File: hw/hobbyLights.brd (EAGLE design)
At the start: 50 x 35.1 mm, 57 parts, among them U1 MCP73831-2, U2 POWER, U3 BD48K28G, U4 ATMEGA32U4-AU, U5 TPS61222, Y1 RESONATORSMD

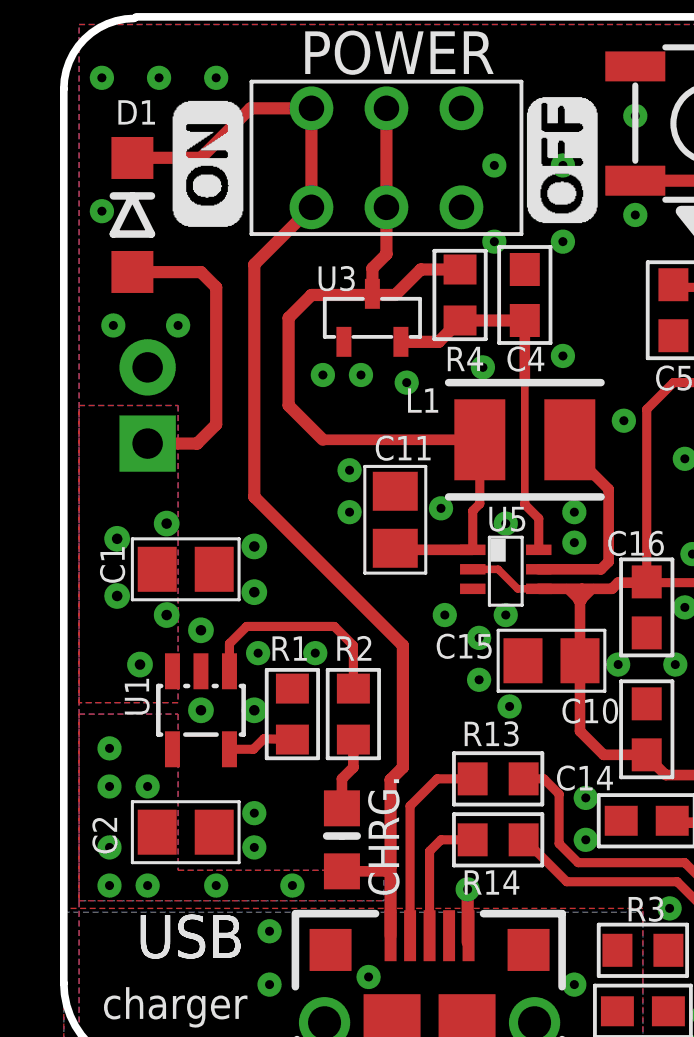
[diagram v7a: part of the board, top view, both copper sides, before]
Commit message: Updated to use JST PH connector. Updates to serigraphy.
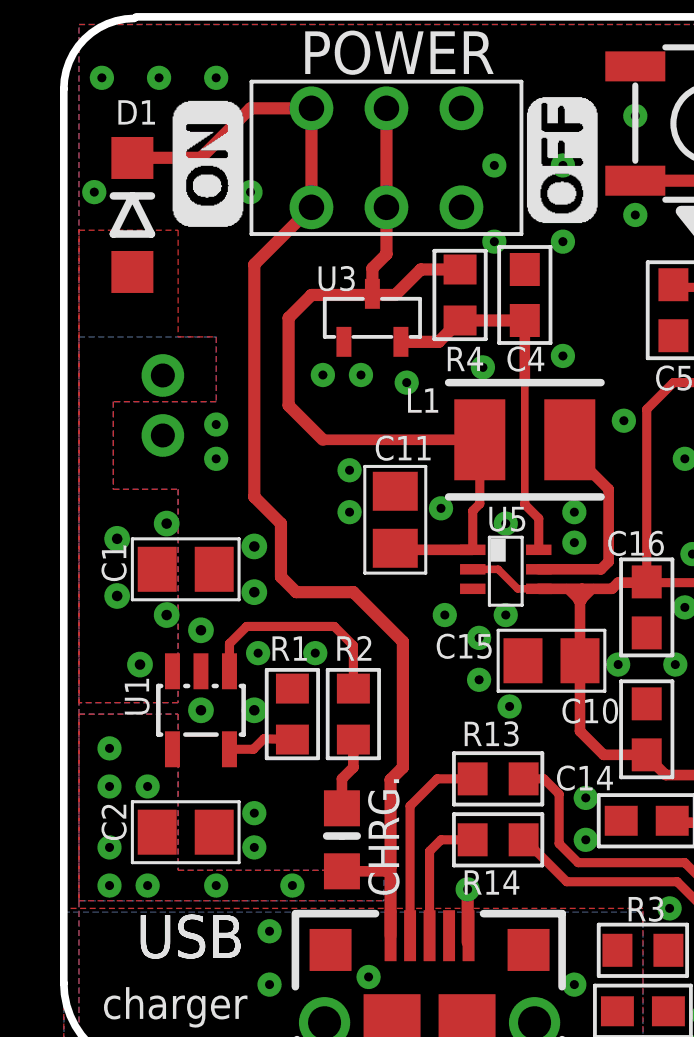
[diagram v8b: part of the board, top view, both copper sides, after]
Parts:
- removed JP1: (no value), SAVLibSAV MK-I:SPARKFUN_MOLEX-1X2
- added CN1: (no value), adafruit:JST-PH-2-THM-RA
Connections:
- net GND: now also CN1.2; no longer JP1.2
- net VCCINT: now also CN1.1; no longer JP1.1
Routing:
- net VCCINT: track 10.1 -> 0.00 mm
- net V_USB: track 38.9 -> 40.0 mm
- net GND: vias 106 -> 107
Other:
- board text added: "B.1"
- board text removed: "B"
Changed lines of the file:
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@@
 <grid distance="0.05" unitdist="inch" unit="mm" style="lines" multiple="1" display="yes" altdistance="5" altunitdist="mil" altunit="mm"/>
 <layers>
-<layer number="1" name="Top" color="4" fill="1" visible="yes" active="yes"/>
+<layer number="1" name="Top" color="4" fill="1" visible="no" active="yes"/>
 <layer number="2" name="Route2" color="1" fill="3" visible="no" active="no"/>
 <layer number="15" name="Route15" color="4" fill="6" visible="no" active="no"/>
-<layer number="16" name="Bottom" color="1" fill="1" visible="no" active="yes"/>
+<layer number="16" name="Bottom" color="1" fill="1" visible="yes" active="yes"/>
 <layer number="17" name="Pads" color="2" fill="1" visible="yes" active="yes"/>
 <layer number="18" name="Vias" color="2" fill="1" visible="yes" active="yes"/>
 <layer number="19" name="Unrouted" color="6" fill="1" visible="yes" active="yes"/>
 <layer number="20" name="Dimension" color="15" fill="1" visible="yes" active="yes"/>
-<layer number="21" name="tPlace" color="7" fill="1" visible="yes" active="yes"/>
-<layer number="22" name="bPlace" color="7" fill="1" visible="no" active="yes"/>
-<layer number="23" name="tOrigins" color="15" fill="1" visible="yes" active="yes"/>
-<layer number="24" name="bOrigins" color="15" fill="1" visible="no" active="yes"/>
-<layer number="25" name="tNames" color="7" fill="1" visible="yes" active="yes"/>
-<layer number="26" name="bNames" color="7" fill="1" visible="no" active="yes"/>
+<layer number="21" name="tPlace" color="7" fill="1" visible="no" active="yes"/>
+<layer number="22" name="bPlace" color="7" fill="1" visible="yes" active="yes"/>
+<layer number="23" name="tOrigins" color="15" fill="1" visible="no" active="yes"/>
+<layer number="24" name="bOrigins" color="15" fill="1" visible="yes" active="yes"/>
+<layer number="25" name="tNames" color="7" fill="1" visible="no" active="yes"/>
+<layer number="26" name="bNames" color="7" fill="1" visible="yes" active="yes"/>
 <layer number="27" name="tValues" color="7" fill="1" visible="no" active="yes"/>
 <layer number="28" name="bValues" color="7" fill="1" visible="no" active="yes"/>
@@
 <wire x1="2.35229375" y1="35" x2="0" y2="32.64770625" width="0.254" layer="20" curve="90"/>
 <wire x1="8.763" y1="7.747" x2="9.779" y2="7.747" width="0.254" layer="21"/>
-<text x="7.747" y="22.606" size="1.778" layer="22" font="vector" ratio="15" rot="MR0">-</text>
-<text x="7.747" y="19.812" size="1.778" layer="22" font="vector" ratio="15" rot="MR0">+</text>
+<text x="6.985" y="18.161" size="2.54" layer="22" font="vector" ratio="15" rot="MR0">-</text>
+<text x="6.985" y="24.13" size="2.54" layer="22" font="vector" ratio="15" rot="MR0">+</text>
 <text x="33.655" y="15.24" size="1.4224" layer="22" font="vector" ratio="12" rot="MR0">hobby lights</text>
-<text x="33.02" y="11.811" size="1.4224" layer="22" font="vector" ratio="12" rot="MR0">B</text>
+<text x="33.02" y="11.811" size="1.4224" layer="22" font="vector" ratio="12" rot="MR0">B.1</text>
 <dimension x1="2.35229375" y1="35" x2="5.08" y2="0" x3="-6.35" y3="17.5" textsize="1.4224" textratio="12" layer="47" dtype="vertical"/>
 <dimension x1="0" y1="32.64770625" x2="50.038" y2="29.21" x3="25.019" y3="39.878" textsize="1.4224" textratio="12" layer="47" dtype="horizontal"/>
@@
 </element>
 <element name="C1" library="rcl" package="C0805" value="4.7uF" x="4.064" y="16.637" smashed="yes">
-<attribute name="NAME" x="2.032" y="16.129" size="0.8128" layer="25" ratio="12" rot="R90"/>
+<attribute name="NAME" x="1.27" y="17.526" size="0.8128" layer="25" ratio="12" rot="R270"/>
 <attribute name="VALUE" x="2.794" y="14.097" size="1.27" layer="27"/>
 </element>
 <element name="C2" library="rcl" package="C0805" value="4.7uF" x="4.064" y="7.874" smashed="yes">
-<attribute name="NAME" x="1.778" y="7.112" size="0.8128" layer="25" ratio="12" rot="R90"/>
+<attribute name="NAME" x="1.27" y="8.89" size="0.8128" layer="25" ratio="12" rot="R270"/>
 <attribute name="VALUE" x="2.794" y="5.334" size="1.27" layer="27"/>
 </element>
@@
 <attribute name="VALUE" x="18.034" y="-0.635" size="1.27" layer="27"/>
 </element>
-<element name="JP1" library="SAVLibSAV MK-I" package="SPARKFUN_MOLEX-1X2" value="" x="2.794" y="20.828" rot="MR90"/>
 <element name="U2" library="fmc" package="SWITCH-JS202011" value="POWER" x="8.255" y="30.353" smashed="yes"/>
 <element name="U$2" library="fmc" package="ON" value="" x="5.969" y="28.067" rot="R90"/>
@@
 <attribute name="NAME" x="31.623" y="1.27" size="0.8128" layer="25" ratio="12"/>
 <attribute name="VALUE" x="27.432" y="-0.254" size="0.8128" layer="27" ratio="12"/>
+</element>
+<element name="CN1" library="adafruit" package="JST-PH-2-THM-RA" value="" x="3.302" y="22.098" smashed="yes" rot="MR90">
+<attribute name="NAME" x="4.097" y="18.425" size="0.8128" layer="26" font="vector" ratio="12" rot="MR0"/>
 </element>
 </elements>
@@
 <via x="13.462" y="5.969" extent="1-16" drill="0.3"/>
 <wire x1="13.462" y1="4.199" x2="13.462" y2="5.969" width="0.4064" layer="1"/>
-<contactref element="JP1" pad="2"/>
 <contactref element="U3" pad="1"/>
 <contactref element="C4" pad="2"/>
@@
 <via x="3.175" y="33.02" extent="1-16" drill="0.3"/>
 <via x="5.08" y="33.02" extent="1-16" drill="0.3"/>
-<via x="1.27" y="28.575" extent="1-16" drill="0.3"/>
-<via x="3.81" y="24.765" extent="1-16" drill="0.3"/>
-<via x="1.651" y="24.765" extent="1-16" drill="0.3"/>
+<via x="1.016" y="29.21" extent="1-16" drill="0.3"/>
 <via x="46.99" y="5.08" extent="1-16" drill="0.3"/>
 <via x="43.18" y="6.35" extent="1-16" drill="0.3"/>
@@
 <via x="39.37" y="22.352" extent="1-16" drill="0.3"/>
 <via x="29.21" y="21.971" extent="1-16" drill="0.3"/>
+<contactref element="CN1" pad="2"/>
+<via x="5.08" y="21.463" extent="1-16" drill="0.3"/>
+<via x="5.08" y="20.32" extent="1-16" drill="0.3"/>
+<via x="6.223" y="29.21" extent="1-16" drill="0.3"/>
 </signal>
 <signal name="N$4">
@@
 <via x="5.08" y="6.096" extent="1-16" drill="0.3"/>
 <via x="7.62" y="6.096" extent="1-16" drill="0.3"/>
-<wire x1="11.303" y1="14.097" x2="11.303" y2="10.033" width="0.4064" layer="1"/>
+<wire x1="11.303" y1="14.224" x2="11.303" y2="10.033" width="0.4064" layer="1"/>
 <contactref element="U2" pad="P4"/>
 <contactref element="U2" pad="P1"/>
 <contactref element="D1" pad="C"/>
-<wire x1="11.303" y1="14.097" x2="6.35" y2="19.05" width="0.4064" layer="1"/>
 <wire x1="8.255" y1="32.003" x2="6.222" y2="32.003" width="0.4064" layer="1"/>
 <wire x1="6.222" y1="32.003" x2="4.572" y2="30.353" width="0.4064" layer="1"/>
@@
 <wire x1="9.271" y1="6.57" x2="10.731" y2="6.57" width="0.3556" layer="1"/>
 <wire x1="10.731" y1="6.57" x2="10.892" y2="6.731" width="0.3556" layer="1"/>
+<wire x1="11.303" y1="14.224" x2="9.652" y2="15.875" width="0.4064" layer="1"/>
+<wire x1="9.652" y1="15.875" x2="7.747" y2="15.875" width="0.4064" layer="1"/>
+<wire x1="7.747" y1="15.875" x2="7.239" y2="16.383" width="0.4064" layer="1"/>
+<wire x1="7.239" y1="16.383" x2="7.239" y2="18.161" width="0.4064" layer="1"/>
+<wire x1="7.239" y1="18.161" x2="6.35" y2="19.05" width="0.4064" layer="1"/>
 </signal>
 <signal name="GND-ISO">
@@
 <signal name="VCCINT" class="1">
 <contactref element="D1" pad="A"/>
-<contactref element="JP1" pad="1"/>
 <contactref element="U1" pad="3"/>
 <contactref element="C1" pad="1"/>
 <polygon width="0.254" layer="1" rank="2">
 <vertex x="0.508" y="12.192"/>
-<vertex x="0.508" y="22.098"/>
-<vertex x="3.81" y="22.098"/>
+<vertex x="0.508" y="27.94"/>
+<vertex x="3.81" y="27.94"/>
+<vertex x="3.81" y="24.384"/>
+<vertex x="5.08" y="24.384"/>
+<vertex x="5.08" y="22.225"/>
+<vertex x="1.651" y="22.225"/>
+<vertex x="1.651" y="19.304"/>
+<vertex x="3.81" y="19.304"/>
 <vertex x="3.81" y="12.192"/>
 </polygon>
 <polygon width="0.254" layer="16" rank="2">
 <vertex x="0.508" y="12.192"/>
-<vertex x="0.508" y="22.098"/>
-<vertex x="3.81" y="22.098"/>
+<vertex x="0.508" y="24.384"/>
+<vertex x="5.08" y="24.384"/>
+<vertex x="5.08" y="22.225"/>
+<vertex x="1.651" y="22.225"/>
+<vertex x="1.651" y="19.304"/>
+<vertex x="3.81" y="19.304"/>
 <vertex x="3.81" y="12.192"/>
 </polygon>
@@
 <via x="3.429" y="15.113" extent="1-16" drill="0.35"/>
 <via x="3.429" y="18.161" extent="1-16" drill="0.35"/>
-<wire x1="2.794" y1="20.828" x2="4.445" y2="20.828" width="0.4064" layer="1"/>
-<wire x1="4.445" y1="20.828" x2="5.08" y2="21.463" width="0.4064" layer="1"/>
-<wire x1="5.08" y1="21.463" x2="5.08" y2="26.035" width="0.4064" layer="1"/>
-<wire x1="5.08" y1="26.035" x2="4.572" y2="26.543" width="0.4064" layer="1"/>
-<wire x1="4.572" y1="26.543" x2="2.799" y2="26.543" width="0.4064" layer="1"/>
-<wire x1="2.799" y1="26.543" x2="2.286" y2="26.548" width="0.4064" layer="1"/>
+<contactref element="CN1" pad="1"/>
 </signal>
 </signals>
